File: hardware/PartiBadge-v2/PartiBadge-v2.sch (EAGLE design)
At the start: 28 parts, among them IC2 TSMP58000, J1 I2C, J2 Supply, U1 1042

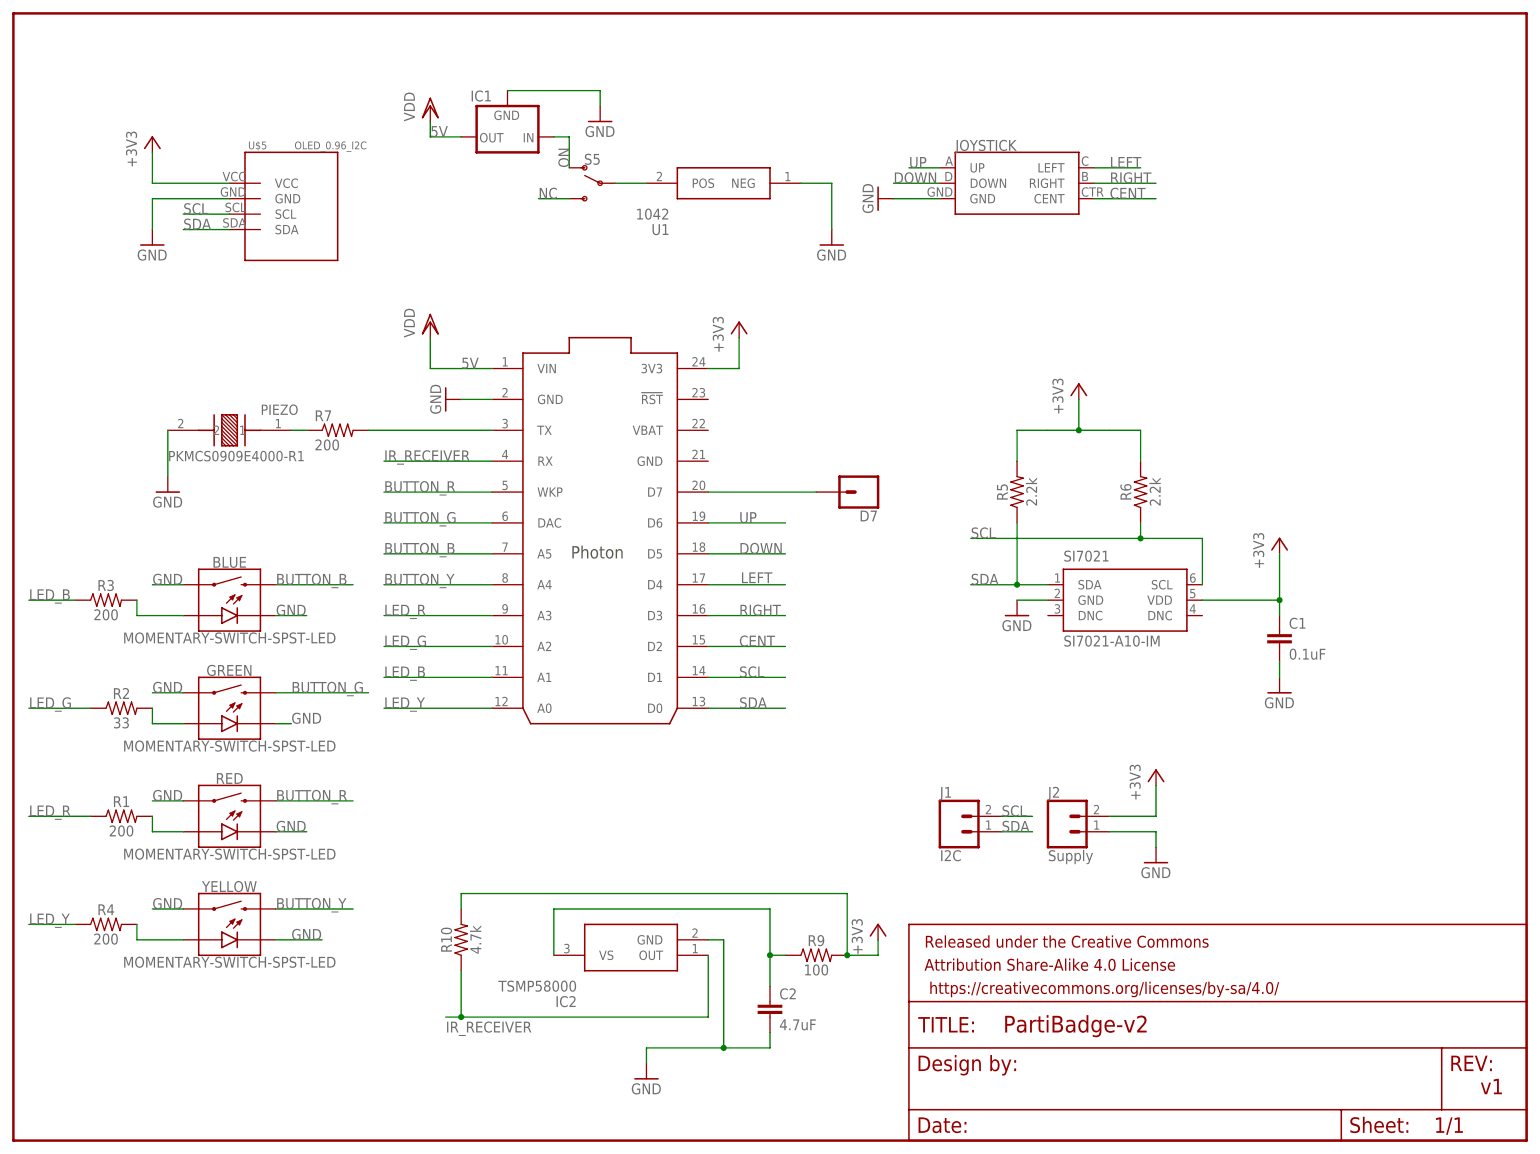
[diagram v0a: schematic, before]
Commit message: added Xenon-based v3 design
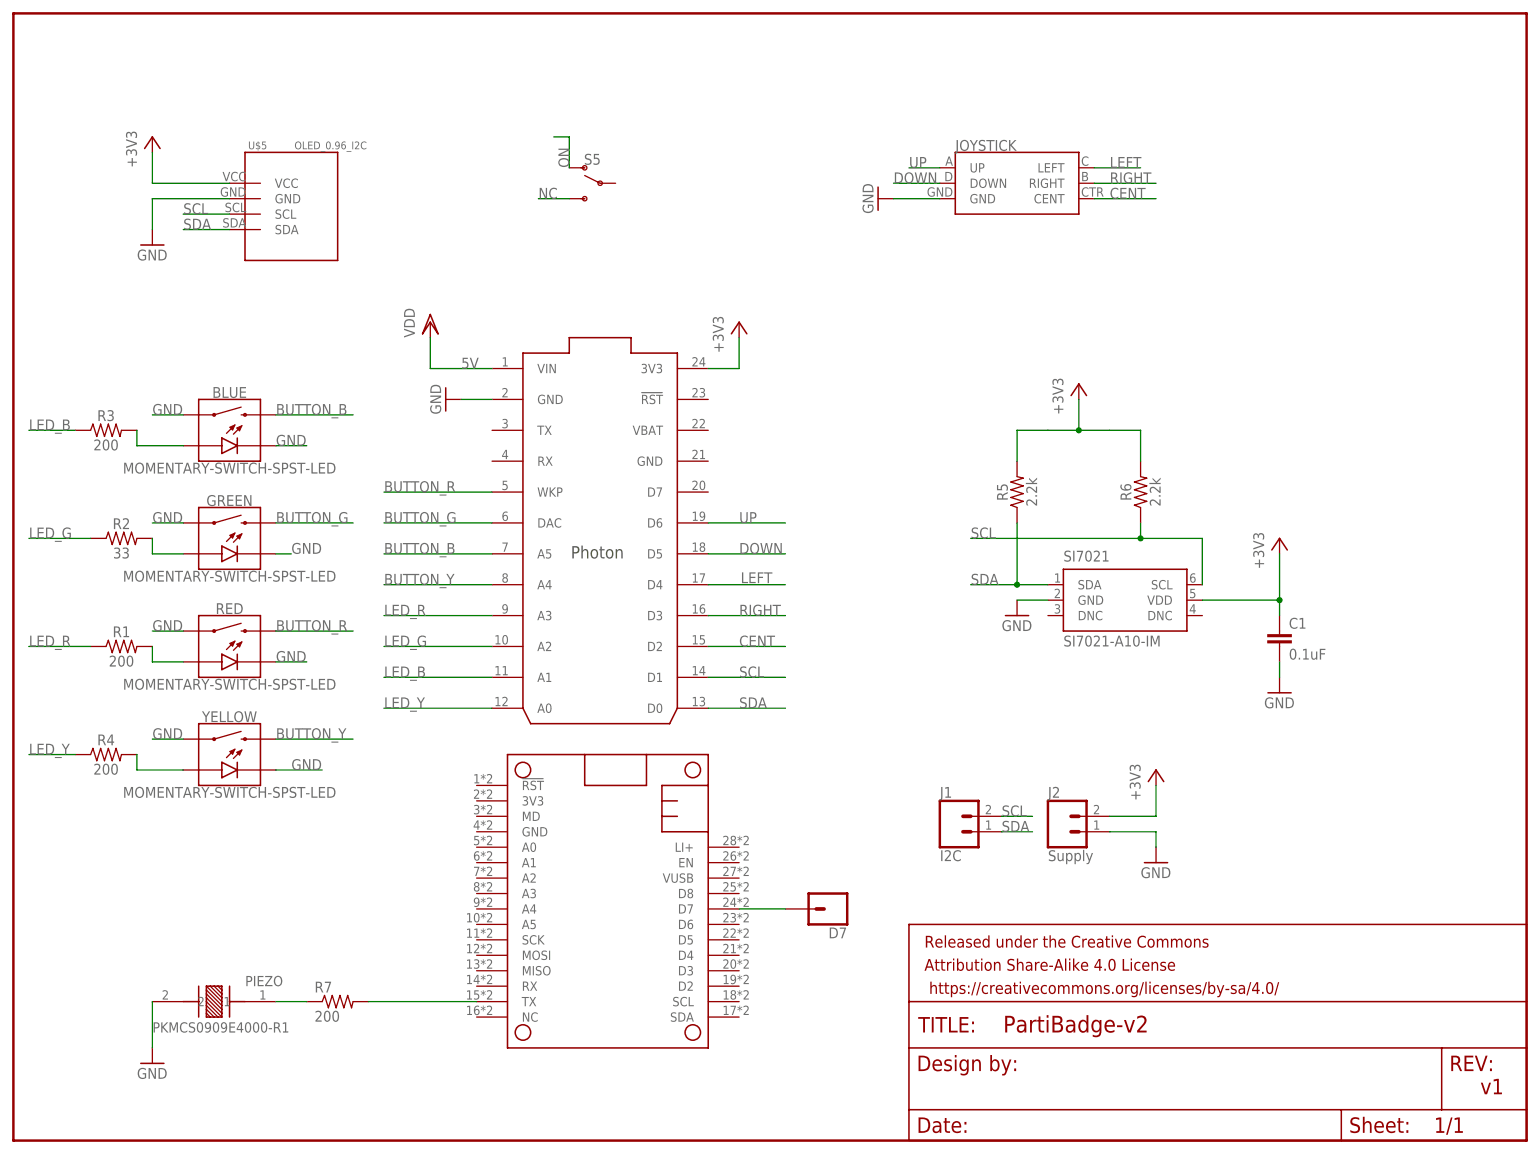
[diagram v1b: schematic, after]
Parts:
- removed C2: 4.7uF, SparkFun-Capacitors:0.1UF-0603-25V-(+80/-20%)
- removed IC1: (no value), v-reg:78XXS
- removed IC2: TSMP58000, TSMP58000:TSMP58000
- removed R10: 4.7k, SparkFun-Resistors:RESISTOR1206
- removed R9: 100, SparkFun-Resistors:RESISTOR1206
- removed U1: 1042, 1042:1042
- added MS1: PARTICLE_MESH_SMTDUAL, Particle-Mesh:PARTICLE_MESH_SMTDUAL
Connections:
- removed net BATT: S5.P, U1.POS
- removed net D7: D7.1, PHOTON.D7
- removed net IR_RECEIVER: IC2.OUT, PHOTON.RX, R10.1
- removed net N$9: C2.1, IC2.VS, R9.1
- new net N$2: MS1.TX, R7.2
- net +3V3: no longer R10.2, R9.2
- net 5V: no longer IC1.OUT
- net GND: no longer C2.2, IC1.GND, IC2.GND, U1.NEG
- net N$1: now also D7.1, MS1.D7; no longer PHOTON.TX, R7.2
- net ON: no longer IC1.IN
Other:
- moved on the sheet: BLUE, D7, GREEN, PIEZO, R1, R2, R3, R4, R7, RED, YELLOW
